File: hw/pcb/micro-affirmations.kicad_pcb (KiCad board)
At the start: 2 copper layers, 100 x 54.5 mm, 148 parts, among them J1 USB-C_2171750001, J2 DEBUG, Q1 SSM3K37FSLF, Q10 SSM3K37FSLF, Q2 SSM3K37FSLF, Q3 SSM3K37FSLF, Q4 SSM3K37FSLF, Q5 SSM3K37FSLF, Q6 SSM3K37FSLF, Q7 SSM3K37FSLF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

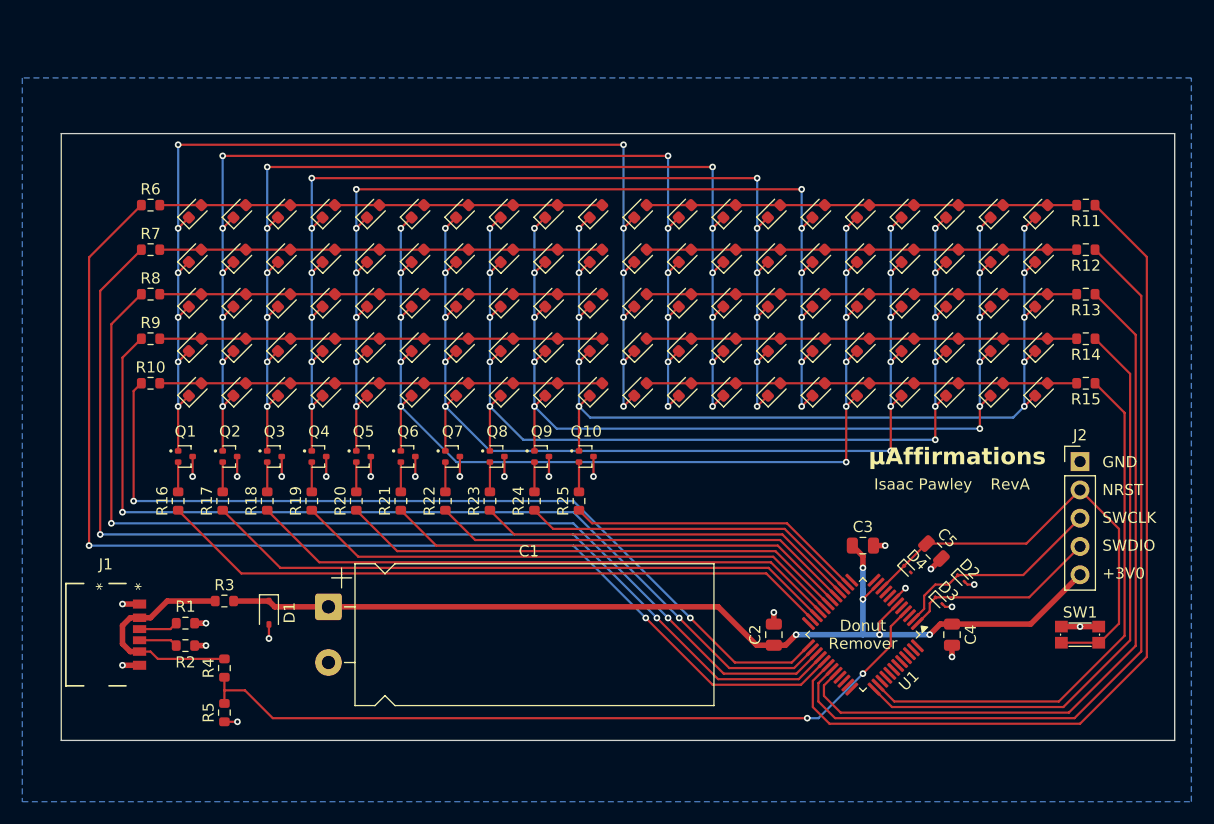
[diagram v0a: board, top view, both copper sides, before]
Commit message: chore: redesigned pcb, new capacitor charger and smaller matrix
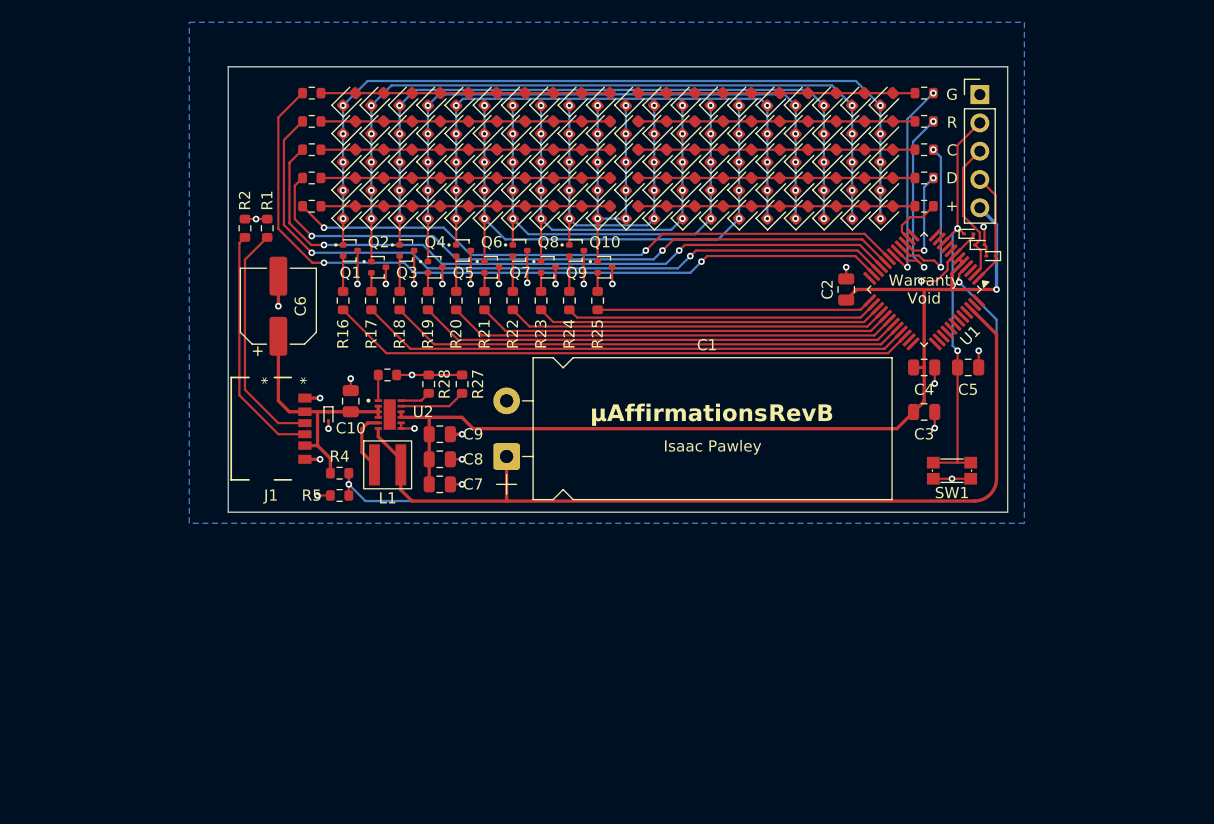
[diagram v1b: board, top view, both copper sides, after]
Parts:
- removed D1: 3V0, Diode_SMD:D_SOD-323
- removed R3: 100, Resistor_SMD:R_0603_1608Metric
- added C10: 10u, Capacitor_SMD:C_0805_2012Metric, F.Cu at (124.5, 114.0)
- added C6: 100u, Capacitor_SMD:CP_Elec_6.3x5.4_Nichicon, F.Cu at (118.0, 105.5)
- added C7: 10u, Capacitor_SMD:C_0805_2012Metric, F.Cu at (132.5, 121.5)
- added C8: 10u, Capacitor_SMD:C_0805_2012Metric, F.Cu at (132.5, 119.2)
- added C9: 10u, Capacitor_SMD:C_0805_2012Metric, F.Cu at (132.5, 117.0)
- added D105: TVS, Diode_SMD:D_SOD-923, F.Cu at (122.5, 115.4)
- added L1: L, micro-affirmations_footprints:L_1616_4040Metric, F.Cu at (127.8, 119.8)
- added R26: 4.75k, Resistor_SMD:R_0603_1608Metric, F.Cu at (127.8, 111.7)
- added R27: 75.0k, Resistor_SMD:R_0603_1608Metric, F.Cu at (134.5, 112.5)
- added R28: 13.0k, Resistor_SMD:R_0603_1608Metric, F.Cu at (131.5, 112.5)
- added U2: TPS61094, micro-affirmations_footprints:WSON_94DSSR_TEX, F.Cu at (128.0, 115.2)
- R10, R11, R12, R13, R14, R15, R6, R7, R8, R9: value R -> 820
- R4, R5: value 10k -> ~
- moved D104 40.0 mm to (149.8, 97.1)
- moved D94 39.5 mm to (149.8, 94.5)
- moved D84 39.0 mm to (149.8, 92.0)
- moved D74 38.5 mm to (149.8, 89.5)
- moved D64 38.1 mm to (149.8, 86.9)
- moved R2 37.9 mm to (115.0, 98.5), turned to 90 degrees
- moved R1 36.2 mm to (117.0, 98.5), turned to 90 degrees
- moved J2 34.2 mm to (181.0, 86.5)
- moved D103 34.1 mm to (152.3, 97.1)
- moved D93 33.5 mm to (152.3, 94.5)
- moved D83 32.9 mm to (152.3, 92.0)
- moved D73 32.3 mm to (152.3, 89.5)
- moved D63 31.8 mm to (152.3, 86.9)
- moved C2 31.7 mm to (169.0, 104.0)
- moved U1 31.5 mm to (176.0, 104.0)
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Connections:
- C1 pad 1: +3V0 -> CAP_VOLT
- C2 pad 1: +3V0 -> +3V3
- C3 pad 1: +3V0 -> +3V3
- C4 pad 1: +3V0 -> +3V3
- J2 pad 5: +3V0 -> +3V3
- U1 pad 11: +3V0 -> unconnected-(U1-PA0-Pad11)
- U1 pad 14: /MATRIX_K9 -> /MATRIX_A9
- U1 pad 15: /MATRIX_K8 -> /MATRIX_A8
- U1 pad 16: /MATRIX_K7 -> /MATRIX_A7
- U1 pad 17: /MATRIX_K6 -> /MATRIX_A6
- U1 pad 18: /MATRIX_K5 -> /MATRIX_A5
- U1 pad 19: /MATRIX_K4 -> /MATRIX_A4
- U1 pad 20: /MATRIX_K3 -> /MATRIX_A3
- U1 pad 21: /MATRIX_K2 -> /MATRIX_A2
- U1 pad 22: /MATRIX_K1 -> /MATRIX_A1
- U1 pad 23: /MATRIX_K0 -> /MATRIX_A0
- U1 pad 25: /MATRIX_A4 -> /MATRIX_K9
- U1 pad 26: /MATRIX_A3 -> /MATRIX_K8
- U1 pad 27: /MATRIX_A2 -> /MATRIX_K7
- U1 pad 28: /MATRIX_A1 -> /MATRIX_K6
- U1 pad 29: /MATRIX_A0 -> /MATRIX_K5
- U1 pad 30: /MATRIX_A5 -> /MATRIX_K4
- U1 pad 31: /MATRIX_A6 -> /MATRIX_K3
- U1 pad 32: /MATRIX_A7 -> /MATRIX_K2
- U1 pad 33: unconnected-(U1-PA11-Pad33) -> /MATRIX_K1
- U1 pad 34: unconnected-(U1-PA12-Pad34) -> /MATRIX_K0
- U1 pad 37: /MATRIX_A8 -> unconnected-(U1-PA15-Pad37)
- U1 pad 38: /MATRIX_A9 -> unconnected-(U1-PD0-Pad38)
- U1 pad 46: unconnected-(U1-PB7-Pad46) -> CAP_VOLT
- U1 pad 5: +3V0 -> +3V3
- U1 pad 6: +3V0 -> +3V3
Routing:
- net +3V0: track 94.8 -> 0.00 mm, vias 5 -> 0
- net +3V3: track 0.00 -> 91.6 mm, vias 0 -> 1
- net CAP_VOLT: track 0.00 -> 78.5 mm
- net Net-(D104-K): track 90.5 -> 26.7 mm
- net Net-(D103-K): track 92.5 -> 30.8 mm, vias 11 -> 10
- net /MATRIX_A5: track 79.9 -> 18.3 mm, vias 0 -> 2
- net Net-(D102-K): track 93.9 -> 37.7 mm, vias 11 -> 10
- net /MATRIX_A6: track 73.3 -> 17.3 mm, vias 0 -> 2
- net Net-(D101-K): track 95.3 -> 41.6 mm, vias 11 -> 10
- net /MATRIX_A7: track 66.7 -> 15.2 mm, vias 0 -> 2
- net Net-(D10-K): track 96.7 -> 48.6 mm, vias 11 -> 10
- net /MATRIX_A8: track 54.5 -> 8.85 mm, vias 0 -> 2
- net Net-(D19-K): track 96.6 -> 51.1 mm, vias 12 -> 10
- net /MATRIX_A9: track 49.0 -> 5.02 mm
- net Net-(D18-K): track 98.6 -> 58.0 mm, vias 12 -> 10
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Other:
- board size 100 x 54.5 mm -> 70 x 40 mm
- board text added: "+"
- board text added: "C"
- board text added: "D"
- board text added: "G"
- board text added: "R"
- board text added: "Warranty Void"
- board text removed: "+3V0"
- board text removed: "Donut Remover"
- board text removed: "GND"
- board text removed: "NRST"
- board text removed: "SWCLK"
- board text removed: "SWDIO"
